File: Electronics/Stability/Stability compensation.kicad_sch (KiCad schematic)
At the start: 5 parts, among them U1 ${SIM.PARAMS}

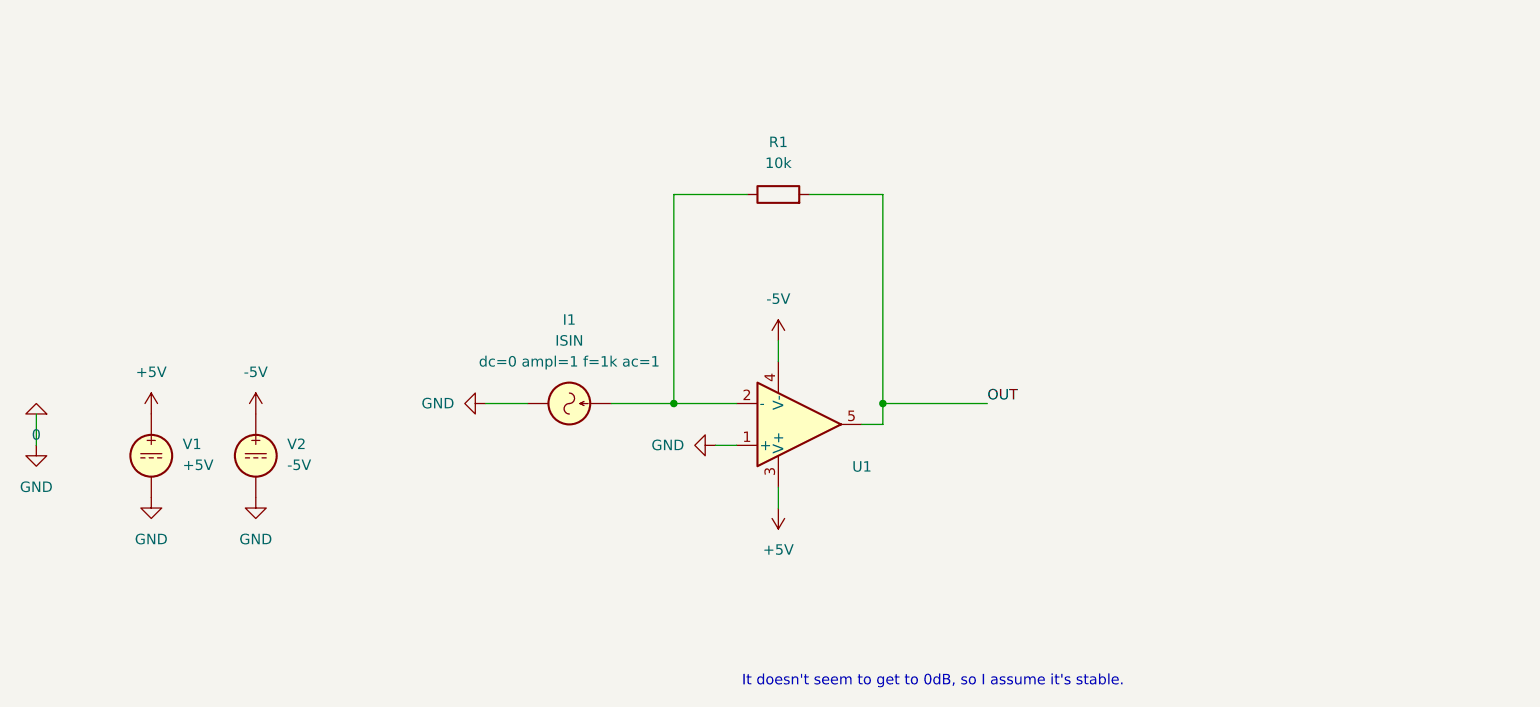
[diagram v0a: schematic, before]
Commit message: Create stability compensation simulation
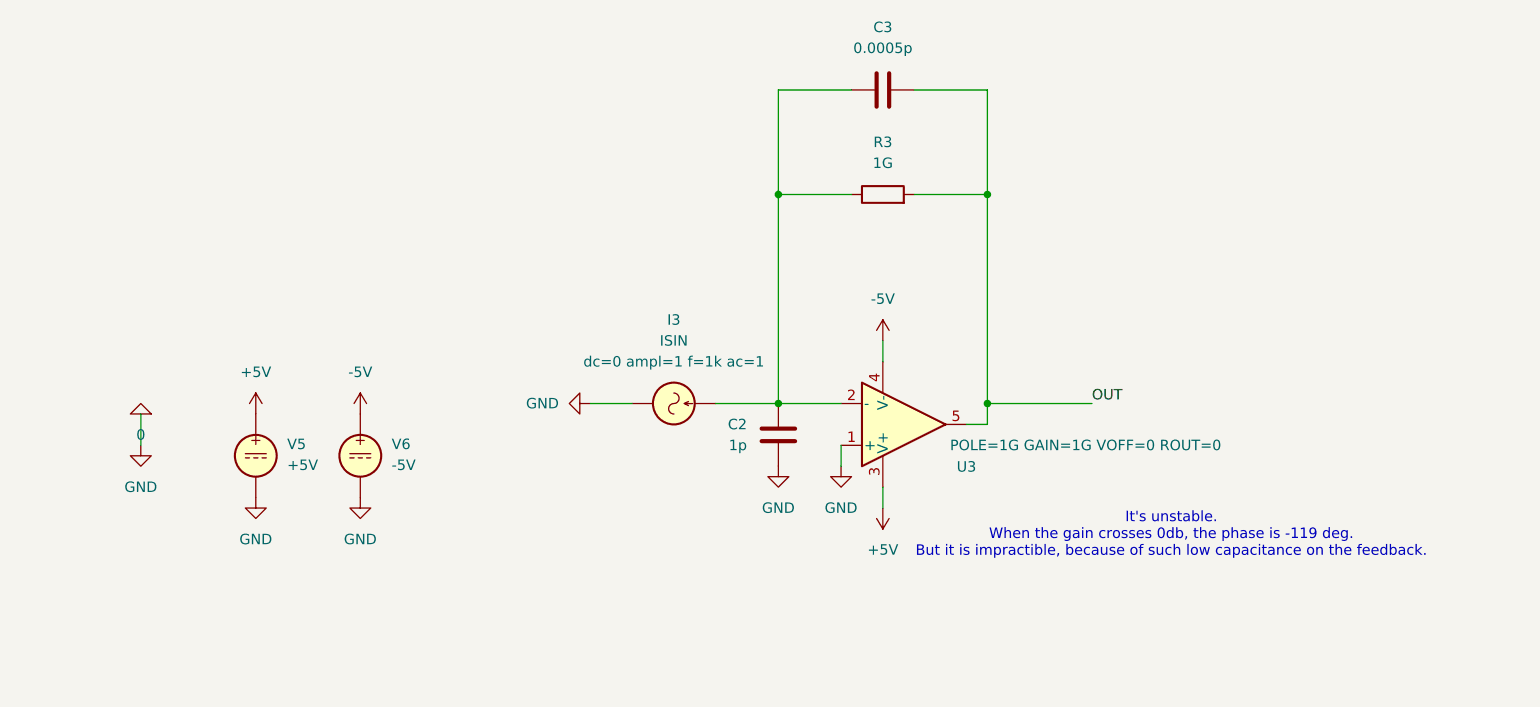
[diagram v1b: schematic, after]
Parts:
- removed I1: ISIN, symbol Simulation_SPICE:ISIN
- removed R1: 10k, symbol Device:R
- removed U1: ${SIM.PARAMS}, symbol Simulation_SPICE:OPAMP
- removed V1: +5V, symbol Simulation_SPICE:VDC
- removed V2: -5V, symbol Simulation_SPICE:VDC
- added C2: 1p, symbol Device:C
- added C3: 0.0005p, symbol Device:C
- added I3: ISIN, symbol Simulation_SPICE:ISIN
- added R3: 1G, symbol Device:R
- added U3: ${SIM.PARAMS}, symbol Simulation_SPICE:OPAMP
- added V5: +5V, symbol Simulation_SPICE:VDC
- added V6: -5V, symbol Simulation_SPICE:VDC
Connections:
- net +5V: now also U3.3 (V+), V5.1
- net -5V: now also U3.4 (V-), V6.1
- net 0: now also C2.2, I3.2, U3.1 (+), V5.2, V6.2
- net OUT: now also C3.2, R3.2, U3.5
- new net: C2.1, C3.1, I3.1, R3.1, U3.2 (-)
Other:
- note added: "It's unstable. When the gain crosses 0db, the phase is -119 deg. But it is impractible, because of such low capacitance on the feedback."
- note removed: "It doesn't seem to get to 0dB, so I assume it's stable."

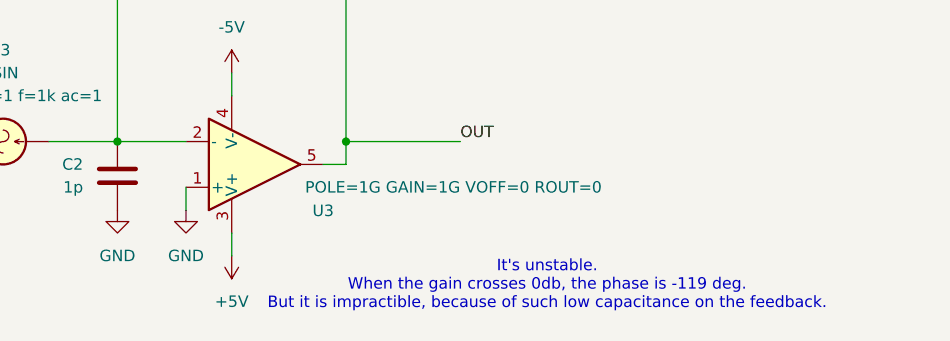
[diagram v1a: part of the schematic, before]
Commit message: Add OPA858 stability simulation
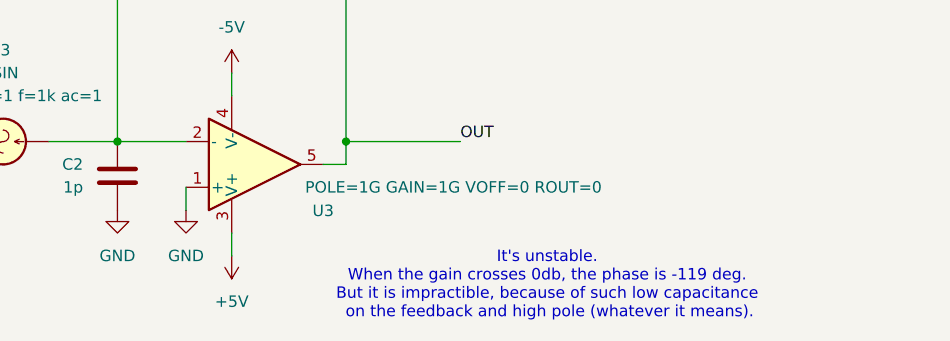
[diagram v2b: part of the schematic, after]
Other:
- note added: "It's unstable. When the gain crosses 0db, the phase is -119 deg. But it is impractible, because of such low capacitance on the feedback and high pole (whatever it means)."
- note removed: "It's unstable. When the gain crosses 0db, the phase is -119 deg. But it is impractible, because of such low capacitance on the feedback."
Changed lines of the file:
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@@
 	(generator_version "10.0")
 	(paper "A4")
-	(text "It's unstable.\nWhen the gain crosses 0db, the phase is -119 deg.\nBut it is impractible, because of such low capacitance on the feedback."
+	(text "It's unstable.\nWhen the gain crosses 0db, the phase is -119 deg.\nBut it is impractible, because of such low capacitance\n on the feedback and high pole (whatever it means)."
 		(exclude_from_sim no)
 		(at 212.852 117.602 0)
